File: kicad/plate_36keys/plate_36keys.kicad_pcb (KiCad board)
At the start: 2 copper layers, 231.6 x 92.5 mm, 54 parts, among them SW1 EC_SW, SW10 EC_SW, SW11 EC_SW, SW12 EC_SW, SW13 EC_SW, SW14 EC_SW, SW15 EC_SW, SW16 EC_SW, SW17 EC_SW, SW18 EC_SW, SW19 EC_SW, SW2 EC_SW, SW20 EC_SW, SW21 EC_SW, SW22 EC_SW, SW23 EC_SW, SW24 EC_SW, SW25 EC_SW, SW26 EC_SW, SW27 EC_SW, SW28 EC_SW, SW29 EC_SW, SW3 EC_SW, SW30 EC_SW, SW31 EC_SW, SW32 EC_SW, SW33 EC_SW, SW34 EC_SW, SW35 EC_SW, SW36 EC_SW, SW4 EC_SW, SW5 EC_SW, SW6 EC_SW, SW7 EC_SW, SW8 EC_SW, SW9 EC_SW

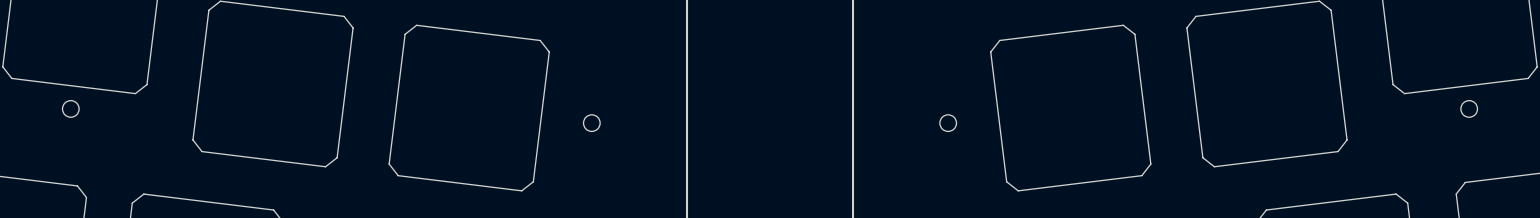
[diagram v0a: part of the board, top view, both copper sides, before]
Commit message: Clean up after prototyping
- Doc update
- remove uncessary files
- remove two more mounting holes in the "chiffre gap" area
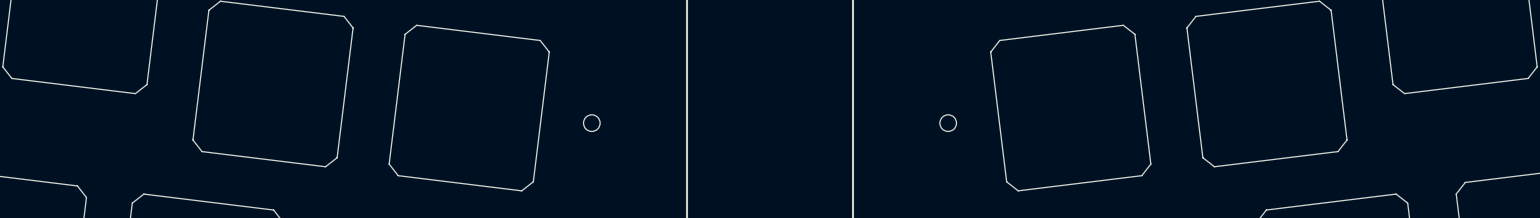
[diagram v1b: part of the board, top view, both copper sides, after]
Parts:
- removed H17, H18: M2 Hole, capacitive_sensors:MountingHole_1.6mm_M2_tapped
- moved H8 132.8 mm to (126.4, 136.8)
- moved H14 122.2 mm to (250.7, 103.0)
- moved H10 97.2 mm to (172.1, 88.6)
- moved H5 94.2 mm to (42.6, 103.0)
- moved H6 89.0 mm to (129.5, 118.4)
- moved H11 88.7 mm to (209.4, 79.2)
- moved H2 71.5 mm to (83.9, 79.2)
- moved H4 50.2 mm to (134.1, 80.6)
- moved H7 49.0 mm to (82.2, 131.8)
- moved H12 47.6 mm to (248.4, 84.1)
- moved H3 38.9 mm to (121.1, 88.6)
- moved H13 18.6 mm to (163.8, 118.4)
- moved H15 18.6 mm to (166.9, 136.8)
- moved H9 15.2 mm to (159.2, 80.6)

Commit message: Remove extra mounting holes from PCB and update version number.
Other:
- board text added: "Le Capybara Plate (36 keys)"
- board text removed: "Le Capybara Plate 36-keys"
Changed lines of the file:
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@@
   (paper "A4")
   (title_block
-    (title "Le Capybara")
-    (date "2023-07-07")
-    (rev "v0.1")
+    (title "Le Capybara Plate (36 keys)")
+    (date "2024-02-21")
+    (rev "1.0")
     (company "sporkus")
   )
@@
     (effects (font (size 2 2) (thickness 0.3)) (justify left bottom))
   )
-  (gr_text "Le Capybara Plate 36-keys" (at 39.880343 56.647143) (layer "User.1")
+  (gr_text "Le Capybara Plate (36 keys)" (at 39.880343 56.647143) (layer "User.1")
     (effects (font (size 4 4) (thickness 0.3)) (justify left bottom))
   )
@@
     (effects (font (size 2 2) (thickness 0.3)) (justify left bottom))
   )
-  (gr_text_box "Drill notes:\n\nA = 16 x M2x0.4mm threaded\nB = 8 x ⌀2.2mm THRU"
+  (gr_text_box "Material thickness: 1.2mm\n\nDrill notes:\n\nA = 16 x M2x0.4mm threaded\nB = 8 x ⌀2.2mm THRU"
     (start 221.917843 143.497143) (end 273.242843 164.897143) (layer "User.1")
       (effects (font (size 2 2) (thickness 0.2)) (justify left top))
